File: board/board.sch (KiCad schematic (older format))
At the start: 16 parts, among them J1 MOTION DETECTOR, J2 EXT BUTTON, J3 GS2, J4 ~POWER, U3 ATTINY85-20PU

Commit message: Add power breakout; updated on-board docs
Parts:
- added J?: GPWR, Pin_Headers:Pin_Header_Straight_1x03_Pitch2.54mm, symbol CONN_01X03
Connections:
- wire segments 48 -> 52
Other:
- note added: "Ambient light sensor"
- note added: "ESP8266 built-in\nRTC auto-reset"
- note added: "Generic external button"
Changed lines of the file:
@@
 NoConn ~ 10050 1700
 NoConn ~ 10050 1800
+Text Notes 5350 2700 0    31   ~ 0
+ESP8266 built-in\nRTC auto-reset
+Text Notes 5900 2700 0    31   ~ 0
+Generic external button
+Text Notes 6600 2700 0    31   ~ 0
+Ambient light sensor
+$Comp
+L CONN_01X03 J?
+U 1 1 5997A27F
+P 4450 1150
+F 0 "J?" H 4450 1350 50  0000 C CNN
+F 1 "GPWR" V 4550 1150 50  0000 C CNN
+F 2 "Pin_Headers:Pin_Header_Straight_1x03_Pitch2.54mm" H 4450 1150 50  0001 C CNN
+F 3 "" H 4450 1150 50  0001 C CNN
+	1    4450 1150
+	0    -1   -1   0
+$EndComp
+$Comp
+L GND #PWR?
+U 1 1 5997A3C4
+P 4550 1650
+F 0 "#PWR?" H 4550 1400 50  0001 C CNN
+F 1 "GND" H 4550 1500 50  0000 C CNN
+F 2 "" H 4550 1650 50  0001 C CNN
+F 3 "" H 4550 1650 50  0001 C CNN
+	1    4550 1650
+	1    0    0    -1
+$EndComp
+Wire Wire Line
+	4550 1650 4550 1350
+$Comp
+L VCC #PWR?
+U 1 1 5997A698
+P 4150 1000
+F 0 "#PWR?" H 4150 850 50  0001 C CNN
+F 1 "VCC" H 4150 1150 50  0000 C CNN
+F 2 "" H 4150 1000 50  0001 C CNN
+F 3 "" H 4150 1000 50  0001 C CNN
+	1    4150 1000
+	1    0    0    -1
+$EndComp
+Wire Wire Line
+	4150 1000 4150 1350
+Wire Wire Line
+	4150 1350 4350 1350
+Wire Wire Line
+	4450 1350 4450 1650
+Text Label 4450 1650 1    60   ~ 0
+VBAT
+Wire Notes Line
+	4000 2750 4000 500
 $EndSCHEMATC

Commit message: Update board to add power breakout
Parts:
- gave numbers to parts that had none: 1
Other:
- note added: "Power breakout"
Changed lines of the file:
@@
 $EndDescr
 $Comp
-L VCC #PWR01
+L VCC #PWR18
 U 1 1 56D753B8
 P 9700 750
-F 0 "#PWR01" H 9700 600 50  0001 C CNN
+F 0 "#PWR18" H 9700 600 50  0001 C CNN
 F 1 "VCC" H 9700 900 50  0000 C CNN
 F 2 "" H 9700 750 50  0000 C CNN
@@
 $EndComp
 $Comp
-L GND #PWR02
+L GND #PWR10
 U 1 1 597CE63C
 P 6700 2000
-F 0 "#PWR02" H 6700 1750 50  0001 C CNN
+F 0 "#PWR10" H 6700 1750 50  0001 C CNN
 F 1 "GND" H 6700 1850 50  0000 C CNN
 F 2 "" H 6700 2000 50  0001 C CNN
@@
 $EndComp
 $Comp
-L VCC #PWR03
+L VCC #PWR9
 U 1 1 597CEF49
 P 6700 1250
-F 0 "#PWR03" H 6700 1100 50  0001 C CNN
+F 0 "#PWR9" H 6700 1100 50  0001 C CNN
 F 1 "VCC" H 6700 1400 50  0000 C CNN
 F 2 "" H 6700 1250 50  0001 C CNN
@@
 $EndComp
 $Comp
-L GND #PWR04
+L GND #PWR11
 U 1 1 597D0A0F
 P 7100 2000
-F 0 "#PWR04" H 7100 1750 50  0001 C CNN
+F 0 "#PWR11" H 7100 1750 50  0001 C CNN
 F 1 "GND" H 7100 1850 50  0000 C CNN
 F 2 "" H 7100 2000 50  0001 C CNN
@@
 $EndComp
 $Comp
-L GND #PWR05
+L GND #PWR15
 U 1 1 597D0EF3
 P 8150 2450
-F 0 "#PWR05" H 8150 2200 50  0001 C CNN
+F 0 "#PWR15" H 8150 2200 50  0001 C CNN
 F 1 "GND" H 8150 2300 50  0000 C CNN
 F 2 "" H 8150 2450 50  0001 C CNN
@@
 $EndComp
 $Comp
-L GND #PWR06
+L GND #PWR8
 U 1 1 597D2087
 P 6250 2000
-F 0 "#PWR06" H 6250 1750 50  0001 C CNN
+F 0 "#PWR8" H 6250 1750 50  0001 C CNN
 F 1 "GND" H 6250 1850 50  0000 C CNN
 F 2 "" H 6250 2000 50  0001 C CNN
@@
 $EndComp
 $Comp
-L GND #PWR07
+L GND #PWR7
 U 1 1 597D12FA
 P 5200 4150
-F 0 "#PWR07" H 5200 3900 50  0001 C CNN
+F 0 "#PWR7" H 5200 3900 50  0001 C CNN
 F 1 "GND" H 5200 4000 50  0000 C CNN
 F 2 "" H 5200 4150 50  0001 C CNN
@@
 $EndComp
 $Comp
-L VCC #PWR08
+L VCC #PWR14
 U 1 1 597D3E37
 P 8000 1850
-F 0 "#PWR08" H 8000 1700 50  0001 C CNN
+F 0 "#PWR14" H 8000 1700 50  0001 C CNN
 F 1 "VCC" H 8000 2000 50  0000 C CNN
 F 2 "" H 8000 1850 50  0001 C CNN
@@
 $EndComp
 $Comp
-L GND #PWR09
+L GND #PWR17
 U 1 1 5986A206
 P 9250 3800
-F 0 "#PWR09" H 9250 3550 50  0001 C CNN
+F 0 "#PWR17" H 9250 3550 50  0001 C CNN
 F 1 "GND" H 9250 3650 50  0000 C CNN
 F 2 "" H 9250 3800 50  0001 C CNN
@@
 $EndComp
 $Comp
-L VCC #PWR010
+L VCC #PWR2
 U 1 1 598F5087
 P 3250 3800
-F 0 "#PWR010" H 3250 3650 50  0001 C CNN
+F 0 "#PWR2" H 3250 3650 50  0001 C CNN
 F 1 "VCC" H 3250 3950 50  0000 C CNN
 F 2 "" H 3250 3800 50  0001 C CNN
@@
 $EndComp
 $Comp
-L VCC #PWR011
+L VCC #PWR1
 U 1 1 598F54B3
 P 3050 3800
-F 0 "#PWR011" H 3050 3650 50  0001 C CNN
+F 0 "#PWR1" H 3050 3650 50  0001 C CNN
 F 1 "VCC" H 3050 3950 50  0000 C CNN
 F 2 "" H 3050 3800 50  0001 C CNN
@@
 $EndComp
 $Comp
-L GND #PWR012
+L GND #PWR16
 U 1 1 598F5F5D
 P 8150 3800
-F 0 "#PWR012" H 8150 3550 50  0001 C CNN
+F 0 "#PWR16" H 8150 3550 50  0001 C CNN
 F 1 "GND" H 8150 3650 50  0000 C CNN
 F 2 "" H 8150 3800 50  0001 C CNN
@@
 $EndComp
 $Comp
-L GND #PWR013
+L GND #PWR13
 U 1 1 598F5FE9
 P 7100 3650
-F 0 "#PWR013" H 7100 3400 50  0001 C CNN
+F 0 "#PWR13" H 7100 3400 50  0001 C CNN
 F 1 "GND" H 7100 3500 50  0000 C CNN
 F 2 "" H 7100 3650 50  0001 C CNN
@@
 $EndComp
 $Comp
-L VCC #PWR014
+L VCC #PWR6
 U 1 1 598F615B
 P 5200 3950
-F 0 "#PWR014" H 5200 3800 50  0001 C CNN
+F 0 "#PWR6" H 5200 3800 50  0001 C CNN
 F 1 "VCC" H 5200 4100 50  0000 C CNN
 F 2 "" H 5200 3950 50  0001 C CNN
@@
 $EndComp
 $Comp
-L VCC #PWR015
+L VCC #PWR12
 U 1 1 598F61A2
 P 7100 3150
-F 0 "#PWR015" H 7100 3000 50  0001 C CNN
+F 0 "#PWR12" H 7100 3000 50  0001 C CNN
 F 1 "VCC" H 7100 3300 50  0000 C CNN
 F 2 "" H 7100 3150 50  0001 C CNN
@@
 $EndComp
 $Comp
-L GND #PWR016
+L GND #PWR19
 U 1 1 598F622C
 P 9700 2500
-F 0 "#PWR016" H 9700 2250 50  0001 C CNN
+F 0 "#PWR19" H 9700 2250 50  0001 C CNN
 F 1 "GND" H 9700 2350 50  0000 C CNN
 F 2 "" H 9700 2500 50  0001 C CNN
@@
 $EndComp
 $Comp
-L GND #PWR017
+L GND #PWR5
 U 1 1 598FDC8B
 P 5050 1600
-F 0 "#PWR017" H 5050 1350 50  0001 C CNN
+F 0 "#PWR5" H 5050 1350 50  0001 C CNN
 F 1 "GND" H 5050 1450 50  0000 C CNN
 F 2 "" H 5050 1600 50  0001 C CNN
@@
 Ambient light sensor
 $Comp
-L CONN_01X03 J?
+L CONN_01X03 J5
 U 1 1 5997A27F
 P 4450 1150
-F 0 "J?" H 4450 1350 50  0000 C CNN
+F 0 "J5" H 4450 1350 50  0000 C CNN
 F 1 "GPWR" V 4550 1150 50  0000 C CNN
 F 2 "Pin_Headers:Pin_Header_Straight_1x03_Pitch2.54mm" H 4450 1150 50  0001 C CNN
@@
 $EndComp
 $Comp
-L GND #PWR?
+L GND #PWR4
 U 1 1 5997A3C4
 P 4550 1650
-F 0 "#PWR?" H 4550 1400 50  0001 C CNN
+F 0 "#PWR4" H 4550 1400 50  0001 C CNN
 F 1 "GND" H 4550 1500 50  0000 C CNN
 F 2 "" H 4550 1650 50  0001 C CNN
@@
 	4550 1650 4550 1350
 $Comp
-L VCC #PWR?
+L VCC #PWR3
 U 1 1 5997A698
 P 4150 1000
-F 0 "#PWR?" H 4150 850 50  0001 C CNN
+F 0 "#PWR3" H 4150 850 50  0001 C CNN
 F 1 "VCC" H 4150 1150 50  0000 C CNN
 F 2 "" H 4150 1000 50  0001 C CNN
@@
 Wire Notes Line
 	4000 2750 4000 500
+Text Notes 4150 2700 0    31   ~ 0
+Power breakout
 $EndSCHEMATC

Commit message: Rework board to use Attiny84
MOAR GPIOS!

* Add battery level monitor
* Move RTC signal to power controller
* Add external wake signal breakout
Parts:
- removed J3: GS2, Connectors:GS2, symbol GS2
- removed U3: ATTINY85-20PU, Housings_SOIC:SOIC-8_3.9x4.9mm_Pitch1.27mm, symbol ATTINY85-20PU
- added J3: EXT WAKE, Pin_Headers:Pin_Header_Straight_1x02_Pitch2.54mm, symbol CONN_01X02
- added R5: 12K, Resistors_SMD:R_0805_HandSoldering, symbol R
- added R7: 30K, Resistors_SMD:R_0805_HandSoldering, symbol R
- added R9: 1K, Resistors_SMD:R_0805_HandSoldering, symbol R
- added U1: ATTINY84-20SSU, Housings_SOIC:SOIC-14_3.9x8.7mm_Pitch1.27mm, symbol ATTINY84-20SSU
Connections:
- net labels added: ATY_MISO, ATY_MOSI, ATY_SCK, BAT_MON, EXT_WAKE, ~ATY_RST
- wire segments 52 -> 55
- no-connect marks 9 -> 12
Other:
- note added: "Battery level monitor"
- note added: "External wake"
- note added: "Power switch"
- note removed: "ESP8266 built-in\nRTC auto-reset"
- moved on the sheet: ISP1, J4, J5, R4, R8

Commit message: Switch footprint part number
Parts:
- U1: value ATTINY84-20SSU -> ATTINY84A-SSU; symbol ATTINY84-20SSU -> ATTINY84A-SSU
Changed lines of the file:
@@
 Power breakout
 $Comp
-L ATTINY84-20SSU U1
+L ATTINY84A-SSU U1
 U 1 1 599A259A
 P 6200 3600
 F 0 "U1" H 5350 4350 50  0000 C CNN
-F 1 "ATTINY84-20SSU" H 6900 2850 50  0000 C CNN
+F 1 "ATTINY84A-SSU" H 6900 2850 50  0000 C CNN
 F 2 "Housings_SOIC:SOIC-14_3.9x8.7mm_Pitch1.27mm" H 6200 3400 50  0001 C CIN
 F 3 "" H 6200 3600 50  0001 C CNN

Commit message: Board revision 2
* Only connect motion detector to power manager
* Move ambient sensor to power manager
* Increase spacing on LEDs; move to hand solder footprint
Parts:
- removed R1: 22.1K, Resistors_SMD:R_0805_HandSoldering, symbol R
- LED1, LED2: footprint CrumpPrints:APA102 -> CrumpPrints:APA102_hand_solder
- U1: value ATTINY84A-SSU -> ATTINY841-SSU; symbol ATTINY84A-SSU -> ATTINY841-SSU
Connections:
- net D5: no longer J1.3 (P3), U1.5 ((PCINT10/CKOUT/OC0A/INT0)PB2)
- net GND: no longer R3.2
- net VCC: now also R3.1
- net AMBIENT: now reaches U1.11 ((PCINT2/~SS~/RXD0/TOCC1/AIN01/ADC2)PA2)
- net AMBIENT: now also R2.1, R3.2
- removed net A0: JP1.12 (P12), R2.1, R3.1
- new net MOTION_SIG: J1.3 (P3), U1.5 ((PCINT10/RXD0/ICP2/CLKO/TOCC7/ADC8)PB2)
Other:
- moved on the sheet: J1, J2, J3, J4, J5, R2, R3, R5, R6, R7, R9

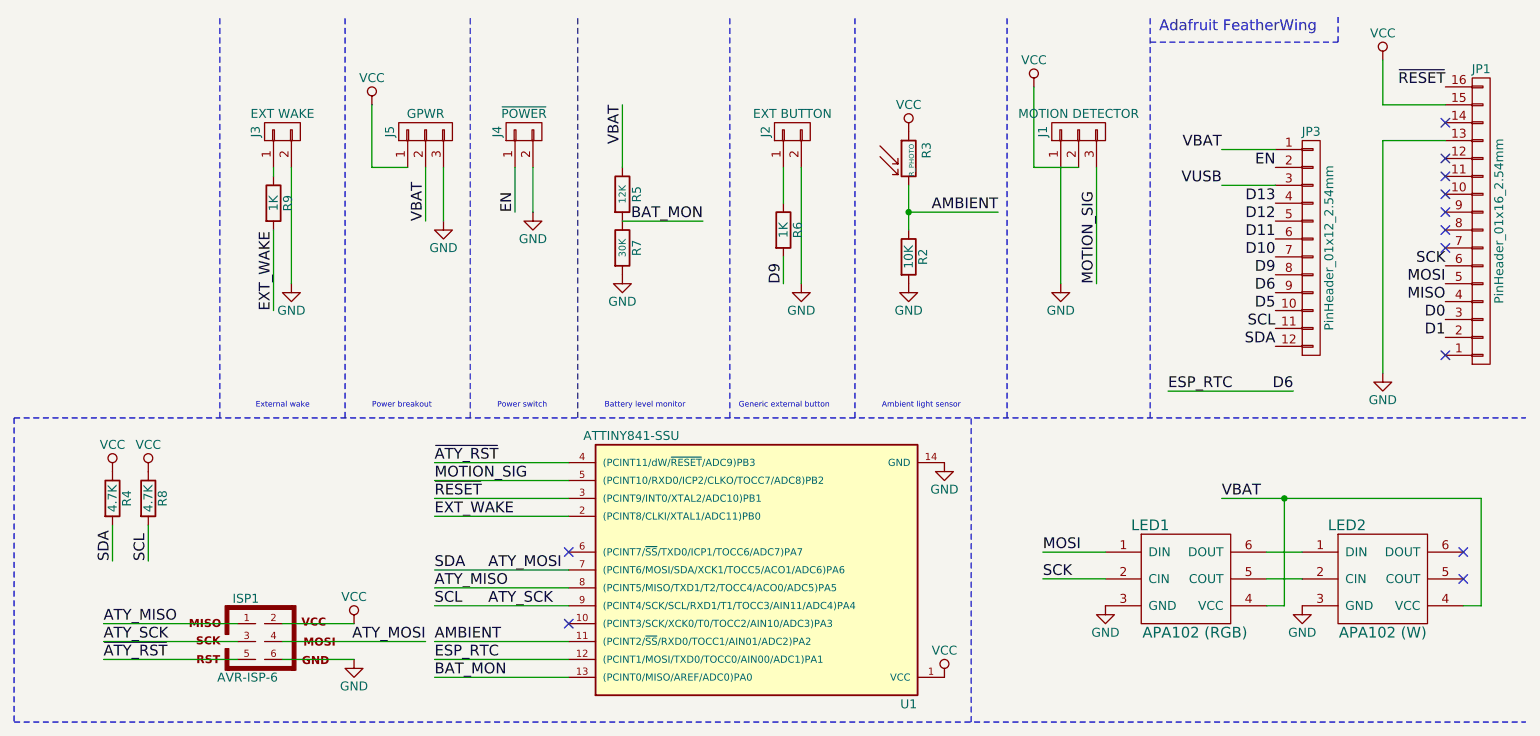
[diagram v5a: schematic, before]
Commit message: Add GPIO header; move attiny further from LEDs
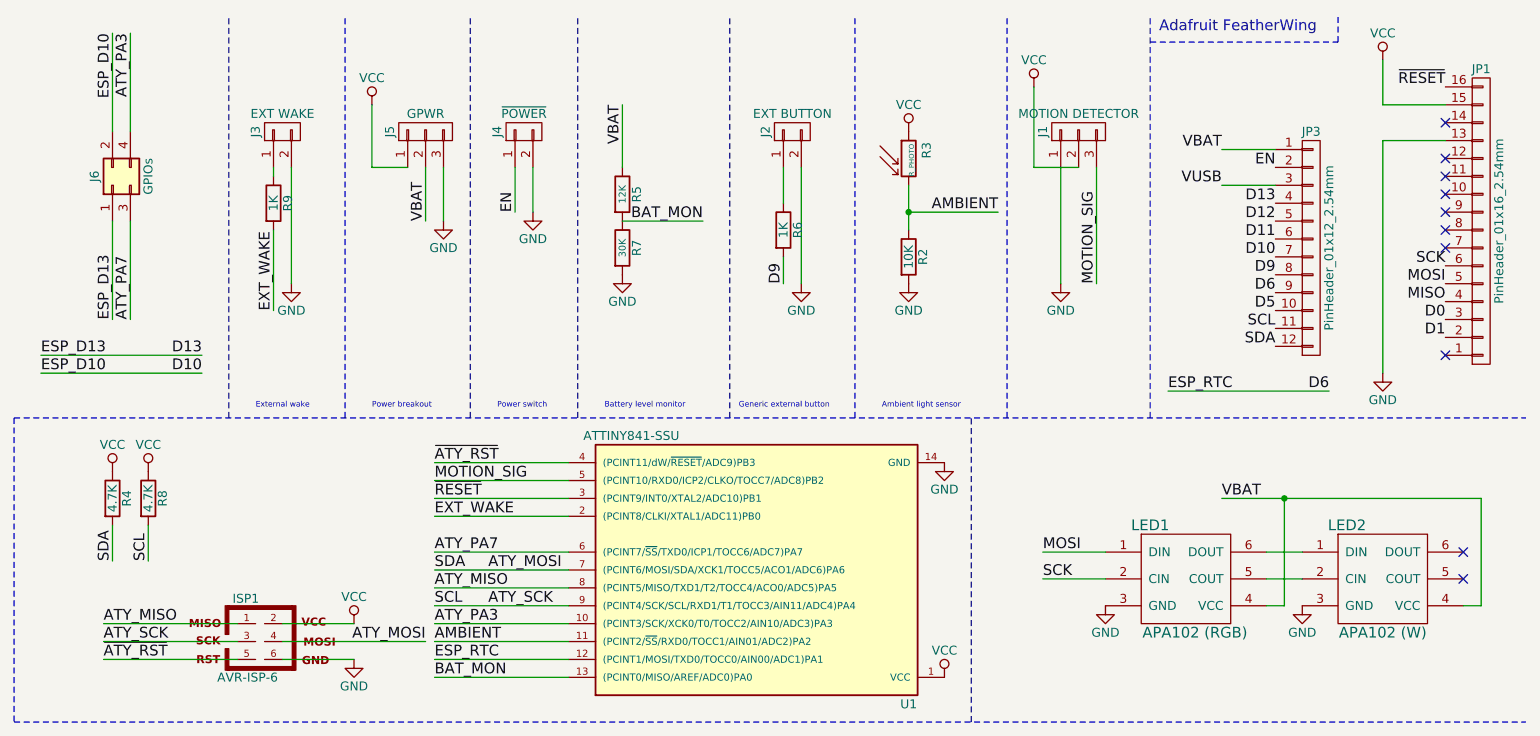
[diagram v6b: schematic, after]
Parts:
- added J6: GPIOs, Pin_Headers:Pin_Header_Straight_2x02_Pitch2.54mm, symbol Conn_02x02_Odd_Even
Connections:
- net D10: now also J6.2 (Pin_2)
- net D13: now also J6.1 (Pin_1)
- net ATY_PA3: now reaches U1.10 ((PCINT3/SCK/XCK0/T0/TOCC2/AIN10/ADC3)PA3)
- net ATY_PA3: now also J6.4 (Pin_4)
- net ATY_PA7: now reaches U1.6 ((PCINT7/~SS~/TXD0/ICP1/TOCC6/ADC7)PA7)
- net ATY_PA7: now also J6.3 (Pin_3)
- no-connect marks 12 -> 10
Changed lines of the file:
@@
 Text Label 2600 3550 1    60   ~ 0
 SDA
-Wire Notes Line
-	2050 2750 10500 2750
-Wire Notes Line
-	8400 2750 8400 500
-Wire Notes Line
-	8400 650  9450 650
-Wire Notes Line
-	9450 650  9450 500
-Wire Wire Line
-	10050 1200 9700 1200
-Wire Wire Line
-	9700 1200 9700 2500
-Wire Wire Line
-	10050 1000 9700 1000
-Wire Wire Line
-	9700 1000 9700 750
-Wire Wire Line
-	9100 1450 8800 1450
-Wire Wire Line
-	9100 1250 8800 1250
-Wire Wire Line
-	7800 3650 8150 3650
-Wire Wire Line
-	7800 3500 8150 3500
-Wire Wire Line
-	9050 3800 9150 3800
-Wire Wire Line
-	9150 3800 9150 3200
-Wire Wire Line
-	8800 3200 10250 3200
-Wire Wire Line
-	10250 3200 10250 3800
-Wire Wire Line
-	10250 3800 10150 3800
-Wire Wire Line
-	9050 3650 9250 3650
-Wire Wire Line
-	9050 3500 9250 3500
-Wire Wire Line
-	7050 1600 7550 1600
-Wire Notes Line
-	7600 2750 7600 500
-Wire Notes Line
-	6750 2750 6750 500
-Wire Notes Line
-	2050 4450 10500 4450
-Wire Notes Line
-	7400 4450 7400 2750
-Wire Wire Line
-	6450 1350 6450 2000
-Wire Wire Line
-	6350 1350 6350 1550
-Wire Notes Line
-	6050 2750 6050 500
-Wire Wire Line
-	7900 2000 7900 1350
-Wire Wire Line
-	8100 1350 8100 2000
-Wire Wire Line
-	6350 1850 6350 2000
-Wire Wire Line
-	2800 3350 2800 3550
-Wire Wire Line
-	2600 3350 2600 3550
-Wire Notes Line
-	2050 2750 2050 4450
-Connection ~ 9150 3200
 NoConn ~ 10050 2400
-Wire Notes Line
-	5200 2750 5200 500
 $Comp
 L CONN_01X02 J4
@@
 	1    0    0    -1
 $EndComp
-Wire Wire Line
-	4850 1350 4850 1600
 Text Label 4850 1600 1    60   ~ 0
 EN
-Wire Wire Line
-	4950 1600 4950 1350
-Wire Notes Line
-	4600 2750 4600 500
 NoConn ~ 10150 3500
 NoConn ~ 10150 3650
@@
 	1    0    0    -1
 $EndComp
-Wire Wire Line
-	4450 1650 4450 1350
 $Comp
 L VCC #PWR015
@@
 	1    0    0    -1
 $EndComp
-Wire Wire Line
-	4050 1000 4050 1350
-Wire Wire Line
-	4050 1350 4250 1350
-Wire Wire Line
-	4350 1350 4350 1650
 Text Label 4350 1650 1    60   ~ 0
 VBAT
-Wire Notes Line
-	3900 2750 3900 500
 Text Notes 4050 2700 0    31   ~ 0
 Power breakout
@@
 	-1   0    0    1
 $EndComp
-Wire Wire Line
-	3550 3900 3950 3900
-Wire Wire Line
-	3550 4100 3950 4100
-Wire Wire Line
-	4400 3800 5150 3800
-Wire Wire Line
-	4400 3600 5150 3600
 Text Label 4400 3600 0    60   ~ 0
 SDA
 Text Label 4400 3000 0    60   ~ 0
 ~ATY_RST
-Wire Wire Line
-	4400 3000 5150 3000
-Wire Wire Line
-	3550 4000 4350 4000
 Text Label 4350 4000 2    60   ~ 0
 ATY_MOSI
-Wire Wire Line
-	5150 3200 4400 3200
-Wire Wire Line
-	5150 3100 4400 3100
-Wire Wire Line
-	3300 4000 2550 4000
 Text Label 2550 4000 0    60   ~ 0
 ATY_SCK
-Wire Wire Line
-	3300 3900 2550 3900
-Wire Wire Line
-	3300 4100 2550 4100
 Text Label 2550 3900 0    60   ~ 0
 ATY_MISO
 Text Label 2550 4100 0    60   ~ 0
 ~ATY_RST
-Wire Wire Line
-	5150 3700 4400 3700
 Text Label 4400 3700 0    60   ~ 0
 ATY_MISO
@@
 	1    0    0    -1
 $EndComp
-Wire Wire Line
-	5450 1350 5450 1000
 Text Label 5450 1000 3    60   ~ 0
 VBAT
-Wire Wire Line
-	5450 1650 5900 1650
 Text Label 5900 1650 2    60   ~ 0
 BAT_MON
@@
 	1    0    0    -1
 $EndComp
-Wire Wire Line
-	5150 4200 4400 4200
 Text Label 4400 4200 0    60   ~ 0
 BAT_MON
-Wire Wire Line
-	5150 4100 4400 4100
 Text Label 4400 4100 0    60   ~ 0
 ESP_RTC
@@
 Text Label 3500 2150 1    60   ~ 0
 EXT_WAKE
-Wire Wire Line
-	3600 1350 3600 2000
-Wire Wire Line
-	3500 1350 3500 1400
-Wire Wire Line
-	3500 1700 3500 2150
-Wire Notes Line
-	3200 2750 3200 500
 Text Notes 3400 2700 0    31   ~ 0
 External wake
-Wire Wire Line
-	5150 3300 4400 3300
 Text Label 4400 3300 0    60   ~ 0
 EXT_WAKE
-NoConn ~ 5150 3500
-NoConn ~ 5150 3900
 Text Label 4700 3600 0    60   ~ 0
 ATY_MOSI
@@
 Text Label 7550 1600 2    60   ~ 0
 AMBIENT
-Wire Wire Line
-	7050 1450 7050 1700
-Connection ~ 7050 1600
 $Comp
 L VCC #PWR018
@@
 	1    0    0    -1
 $EndComp
-Wire Wire Line
-	7750 900  7750 1350
-Wire Wire Line
-	7750 1350 8000 1350
 NoConn ~ 10050 1300
-Wire Wire Line
-	5150 4000 4400 4000
 Text Label 4400 4000 0    60   ~ 0
 AMBIENT
-Wire Wire Line
-	8500 2600 9200 2600
-Text Label 9200 2600 2    60   ~ 0
+Text Label 9400 2600 2    60   ~ 0
 D6
 Text Label 8500 2600 0    60   ~ 0
 ESP_RTC
+Text Label 4400 3500 0    60   ~ 0
+ATY_PA7
+Text Label 4400 3900 0    60   ~ 0
+ATY_PA3
+Wire Notes Line
+	2050 2750 10500 2750
+Wire Notes Line
+	8400 2750 8400 500
+Wire Notes Line
+	8400 650  9450 650
+Wire Notes Line
+	9450 650  9450 500
+Wire Wire Line
+	10050 1200 9700 1200
+Wire Wire Line
+	9700 1200 9700 2500
+Wire Wire Line
+	10050 1000 9700 1000
+Wire Wire Line
+	9700 1000 9700 750
+Wire Wire Line
+	9100 1450 8800 1450
+Wire Wire Line
+	9100 1250 8800 1250
+Wire Wire Line
+	7800 3650 8150 3650
+Wire Wire Line
+	7800 3500 8150 3500
+Wire Wire Line
+	9050 3800 9150 3800
+Wire Wire Line
+	9150 3800 9150 3200
+Wire Wire Line
+	8800 3200 10250 3200
+Wire Wire Line
+	10250 3200 10250 3800
+Wire Wire Line
+	10250 3800 10150 3800
+Wire Wire Line
+	9050 3650 9250 3650
+Wire Wire Line
+	9050 3500 9250 3500
+Wire Wire Line
+	7050 1600 7550 1600
+Wire Notes Line
+	7600 2750 7600 500
+Wire Notes Line
+	6750 2750 6750 500
+Wire Notes Line
+	2050 4450 10500 4450
+Wire Notes Line
+	7400 4450 7400 2750
+Wire Wire Line
+	6450 1350 6450 2000
+Wire Wire Line
+	6350 1350 6350 1550
+Wire Notes Line
+	6050 2750 6050 500
+Wire Wire Line
+	7900 2000 7900 1350
+Wire Wire Line
+	8100 1350 8100 2000
+Wire Wire Line
+	6350 1850 6350 2000
+Wire Wire Line
+	2800 3350 2800 3550
+Wire Wire Line
+	2600 3350 2600 3550
+Wire Notes Line
+	2050 2750 2050 4450
+Connection ~ 9150 3200
+Wire Notes Line
+	5200 2750 5200 500
+Wire Wire Line
+	4850 1350 4850 1600
+Wire Wire Line
+	4950 1600 4950 1350
+Wire Notes Line
+	4600 2750 4600 500
+Wire Wire Line
+	4450 1650 4450 1350
+Wire Wire Line
+	4050 1000 4050 1350
+Wire Wire Line
+	4050 1350 4250 1350
+Wire Wire Line
+	4350 1350 4350 1650
+Wire Notes Line
+	3900 2750 3900 500
+Wire Wire Line
+	3550 3900 3950 3900
+Wire Wire Line
+	3550 4100 3950 4100
+Wire Wire Line
+	4400 3800 5150 3800
+Wire Wire Line
+	4400 3600 5150 3600
+Wire Wire Line
+	4400 3000 5150 3000
+Wire Wire Line
+	3550 4000 4350 4000
+Wire Wire Line
+	5150 3200 4400 3200
+Wire Wire Line
+	5150 3100 4400 3100
+Wire Wire Line
+	3300 4000 2550 4000
+Wire Wire Line
+	3300 3900 2550 3900
+Wire Wire Line
+	3300 4100 2550 4100
+Wire Wire Line
+	5150 3700 4400 3700
+Wire Wire Line
+	5450 1350 5450 1000
+Wire Wire Line
+	5450 1650 5900 1650
+Wire Wire Line
+	5150 4200 4400 4200
+Wire Wire Line
+	5150 4100 4400 4100
+Wire Wire Line
+	3600 1350 3600 2000
+Wire Wire Line
+	3500 1350 3500 1400
+Wire Wire Line
+	3500 1700 3500 2150
+Wire Notes Line
+	3250 2750 3250 500
+Wire Wire Line
+	5150 3300 4400 3300
+Wire Wire Line
+	7050 1450 7050 1700
+Connection ~ 7050 1600
+Wire Wire Line
+	7750 900  7750 1350
+Wire Wire Line
+	7750 1350 8000 1350
+Wire Wire Line
+	5150 4000 4400 4000
+Wire Wire Line
+	8500 2600 9400 2600
+Wire Wire Line
+	5150 3500 4400 3500
+Wire Wire Line
+	5150 3900 4400 3900
+Wire Wire Line
+	3100 2400 2200 2400
+Text Label 3100 2400 2    60   ~ 0
+D13
+Text Label 2200 2400 0    60   ~ 0
+ESP_D13
+Wire Wire Line
+	3100 2500 2200 2500
+Text Label 2200 2500 0    60   ~ 0
+ESP_D10
+Text Label 3100 2500 2    60   ~ 0
+D10
+$Comp
+L Conn_02x02_Odd_Even J6
+U 1 1 59C87DF0
+P 2600 1450
+F 0 "J6" H 2650 1550 50  0000 C CNN
+F 1 "GPIOs" H 2650 1250 50  0000 C CNN
+F 2 "Pin_Headers:Pin_Header_Straight_2x02_Pitch2.54mm" H 2600 1450 50  0001 C CNN
+F 3 "" H 2600 1450 50  0001 C CNN
+	1    2600 1450
+	0    -1   -1   0
+$EndComp
+Wire Wire Line
+	2600 1650 2600 2200
+Text Label 2600 2200 1    60   ~ 0
+ESP_D13
+Wire Wire Line
+	2700 1650 2700 2200
+Text Label 2700 2200 1    60   ~ 0
+ATY_PA7
+Wire Wire Line
+	2600 1150 2600 600
+Text Label 2600 600  3    60   ~ 0
+ESP_D10
+Wire Wire Line
+	2700 1150 2700 600
+Text Label 2700 600  3    60   ~ 0
+ATY_PA3
 $EndSCHEMATC
